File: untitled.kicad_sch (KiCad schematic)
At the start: 16 parts, among them J3 J_000001, J5 J_000002, U2 PWR_nPM1100-QDXX

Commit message: added test points
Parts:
- added TP1: TestPoint VDD, TestPoint:TestPoint_Pad_D1.5mm, symbol Connector:TestPoint
- added TP2: TestPoint GND, TestPoint:TestPoint_Pad_D1.5mm, symbol Connector:TestPoint
- added TP3: TestPoint VBAT, TestPoint:TestPoint_Pad_D1.5mm, symbol Connector:TestPoint
- added TP4: TestPoint VBUS, TestPoint:TestPoint_Pad_D1.5mm, symbol Connector:TestPoint
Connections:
- net +3V0 VDD_NRF: now also TP1.1
- net GND: now also TP2.1
- net VBAT: now also TP3.1
- net VBUS: now also TP4.1
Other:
- moved on the sheet: C17

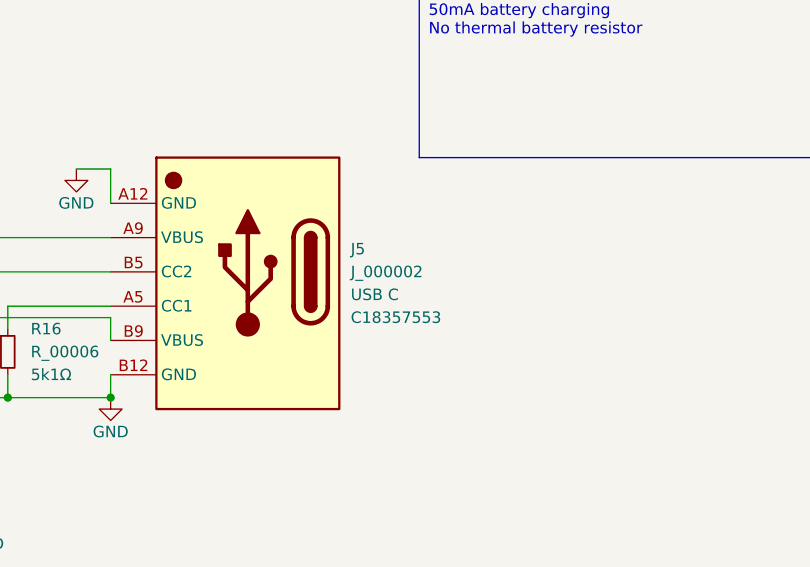
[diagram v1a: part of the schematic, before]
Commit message: fixed ERC errors
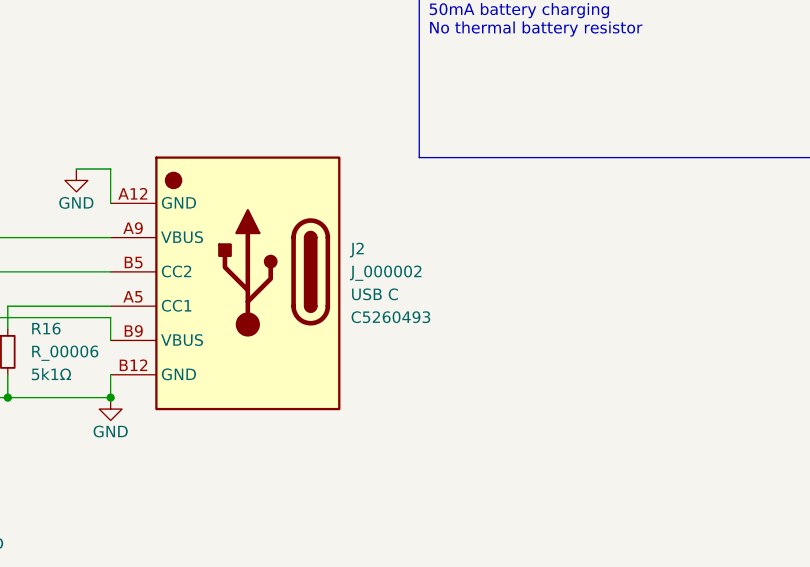
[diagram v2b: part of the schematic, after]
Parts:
- removed J5: J_000002, mic_patch_parts:C5260493, symbol mic_patch_parts:1000009
- added J2: J_000002, mic_patch_parts:J_000002, symbol mic_patch_parts:J_000002
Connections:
- net GND: now also J2.A12 (GND), J2.B12 (GND)
- net VBUS: now also J2.A9 (VBUS), J2.B9 (VBUS)
- net at R16.1: now also J2.A5 (CC1)
- net at R14.1: now also J2.B5 (CC2)
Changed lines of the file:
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@@
 	)
 	(symbol
-		(lib_id "mic_patch_parts:1000009")
+		(lib_id "mic_patch_parts:J_000002")
 		(at 193.04 62.23 0)
 		(unit 1)
@@
 		(dnp no)
 		(fields_autoplaced yes)
-		(property "Reference" "J5"
+		(property "Reference" "J2"
 			(at 207.01 55.8799 0)
 			(effects
@@
 			)
 		)
-		(property "Footprint" "mic_patch_parts:C5260493"
+		(property "Footprint" "mic_patch_parts:J_000002"
 			(at 194.564 78.232 0)
 			(effects
@@
 			)
 		)
-		(property "LCSC PNs" "C18357553"
+		(property "LCSC PNs" "C5260493"
 			(at 207.01 63.4999 0)
 			(effects
@@
 			)
 		)
+		(pin "A9"
+		)
+		(pin "B12"
+		)
 		(pin "B5"
+		)
+		(pin "B9"
 		)
 		(pin "A5"
@@
 		(pin "A12"
 		)
-		(pin "A9"
-		)
-		(pin "B12"
-		)
-		(pin "B12"
-		)
-		(pin "B9"
-		)
-		(pin "B9"
-		)
 		(instances
 			(project "mic_patch_v1"
 				(path "/5448a297-4261-40a5-8009-47199bfe22cb/549bd3f0-5402-4113-b11d-8a88b4fc0730"
-					(reference "J5")
+					(reference "J2")
 					(unit 1)
 				)

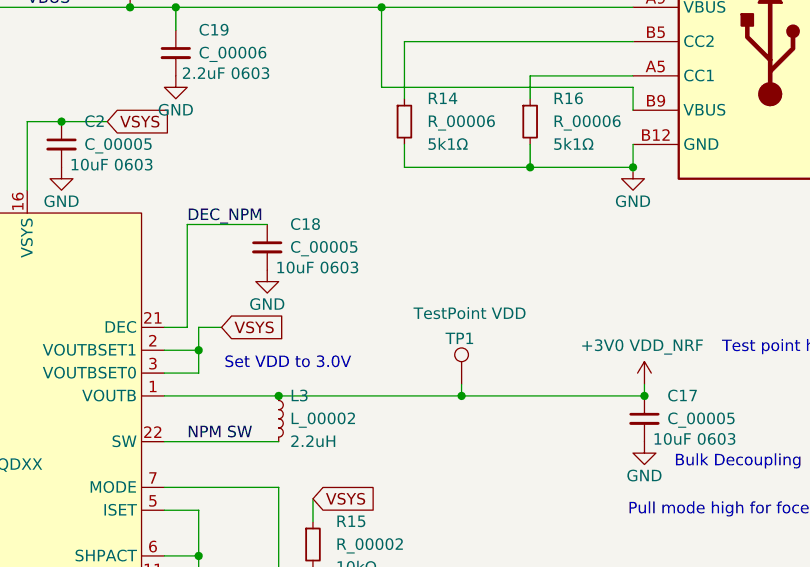
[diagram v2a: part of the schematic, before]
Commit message: poured ground layer added RF keep out
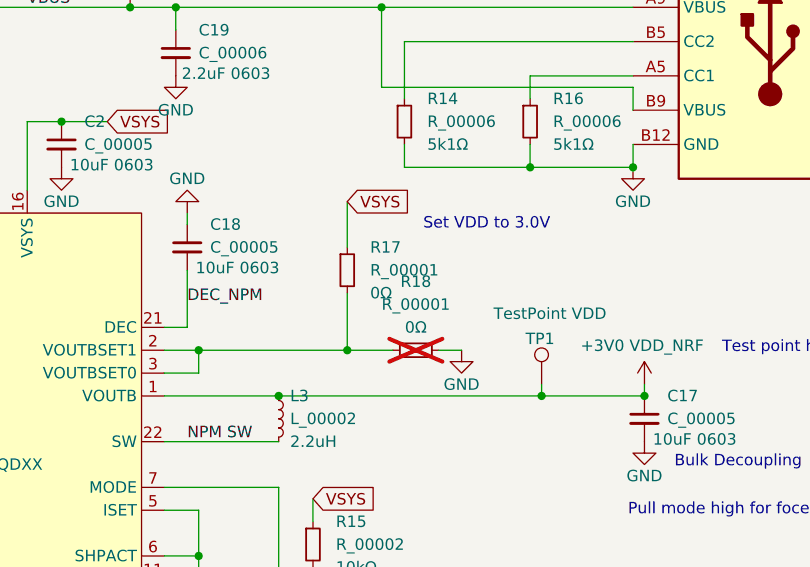
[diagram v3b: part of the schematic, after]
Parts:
- added R17, R18: R_00001, Resistor_SMD:R_0805_2012Metric, symbol mic_patch_parts:R_00001
- TP1, TP2, TP3, TP4: footprint TestPoint:TestPoint_Pad_D1.5mm -> TestPoint:TestPoint_Pad_D1.0mm
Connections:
- net DEC_NPM: now also C18.2; no longer C18.1
- net GND: now also C18.1, R18.1; no longer C18.2
- net VSYS: now also R17.1; no longer U2.2 (VOUTBSET1), U2.3 (VOUTBSET0)
- new net: R17.2, R18.2, U2.2 (VOUTBSET1), U2.3 (VOUTBSET0)
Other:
- moved on the sheet: C18, TP1

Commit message: re-routed buttons to closer pins
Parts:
- TP1, TP2: footprint TestPoint:TestPoint_Pad_D1.0mm -> TestPoint:TestPoint_Pad_D1.5mm
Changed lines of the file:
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@@
 			)
 		)
-		(property "Footprint" "TestPoint:TestPoint_Pad_D1.0mm"
+		(property "Footprint" "TestPoint:TestPoint_Pad_D1.5mm"
 			(at 175.26 96.52 0)
 			(effects
@@
 			)
 		)
-		(property "Footprint" "TestPoint:TestPoint_Pad_D1.0mm"
+		(property "Footprint" "TestPoint:TestPoint_Pad_D1.5mm"
 			(at 118.11 140.97 0)
 			(effects

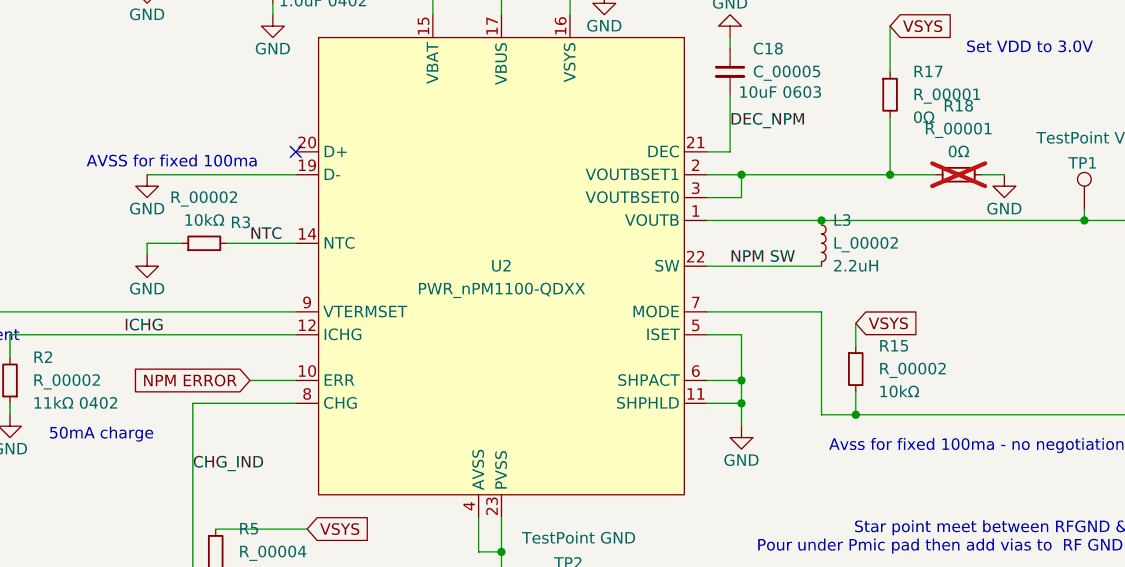
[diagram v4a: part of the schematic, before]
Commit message: corrected missing part numbers + inconsistencies
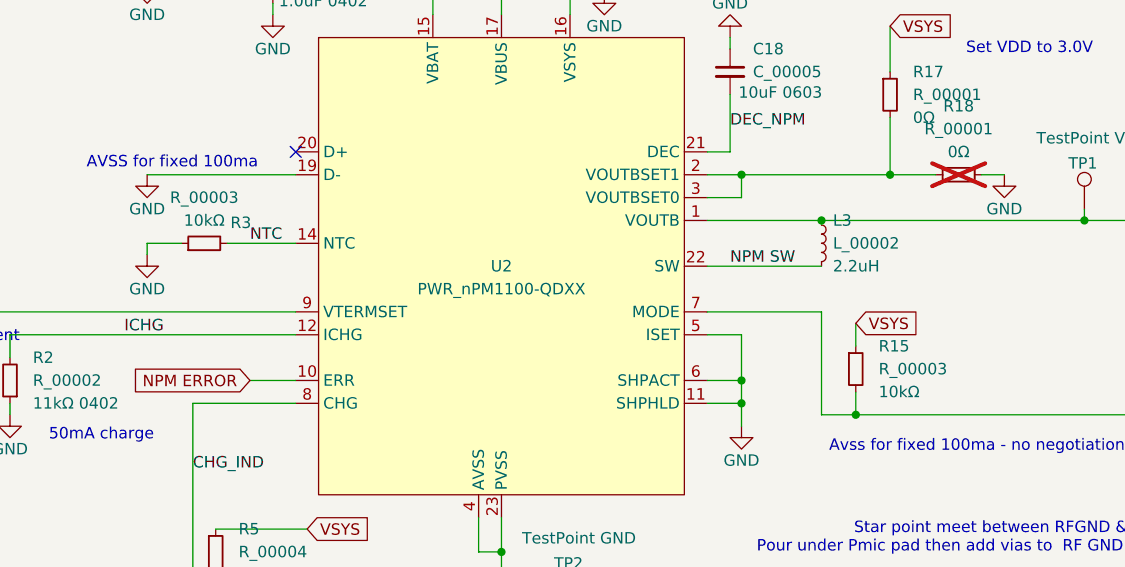
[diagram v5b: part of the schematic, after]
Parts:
- R15, R3: value R_00002 -> R_00003
- R17: LCSC PNs (none) -> C17477
- U2: LCSC PNs (none) -> C7249860
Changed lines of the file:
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@@
 	)
 	(symbol
+		(lib_name "R_00003_1")
 		(lib_id "mic_patch_parts:R_00003")
 		(at 144.78 114.3 0)
@@
 			)
 		)
-		(property "Value" "R_00002"
+		(property "Value" "R_00003"
 			(at 147.32 114.2999 0)
 			(effects
@@
 			)
 		)
-		(property "Value" "R_00002"
+		(property "Value" "R_00003"
 			(at 72.39 95.25 90)
 			(effects
@@
 			)
 		)
+		(property "LCSC PNs" "C7249860"
+			(at 105.41 102.87 0)
+			(effects
+				(font
+					(size 1.27 1.27)
+				)
+				(hide yes)
+			)
+		)
 		(pin "10"
 		)
@@
 	)
 	(symbol
+		(lib_name "R_00001_1")
 		(lib_id "mic_patch_parts:R_00001")
 		(at 148.59 83.82 0)
@@
 			)
 		)
-		(property "LCSC PNs" ""
+		(property "LCSC PNs" "C17477"
 			(at 148.59 83.82 0)
 			(effects

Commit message: updated footprint for C19, corrected
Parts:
- C19: footprint Capacitor_SMD:C_0201_0603Metric -> Capacitor_SMD:C_0603_1608Metric
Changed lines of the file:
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@@
 			)
 		)
-		(property "Footprint" "Capacitor_SMD:C_0201_0603Metric"
+		(property "Footprint" "Capacitor_SMD:C_0603_1608Metric"
 			(at 104.14 60.96 0)
 			(effects

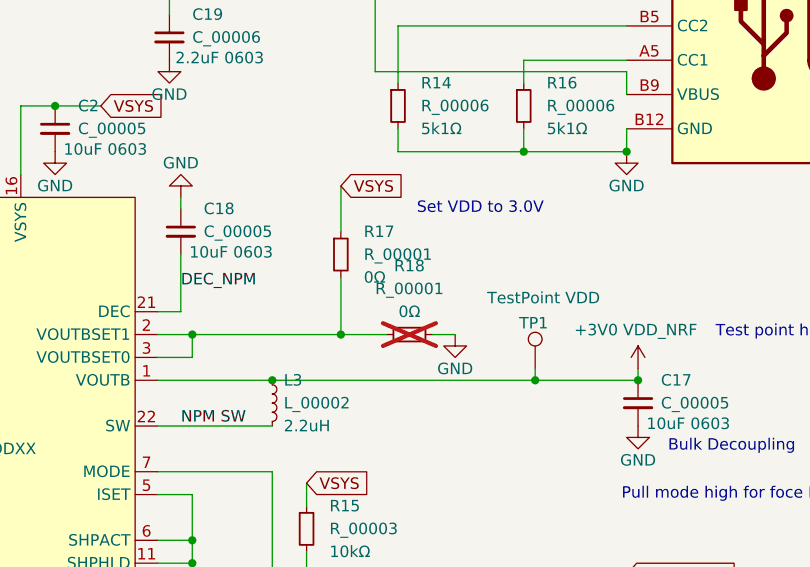
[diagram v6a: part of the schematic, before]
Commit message: Removed SD Card from schematic
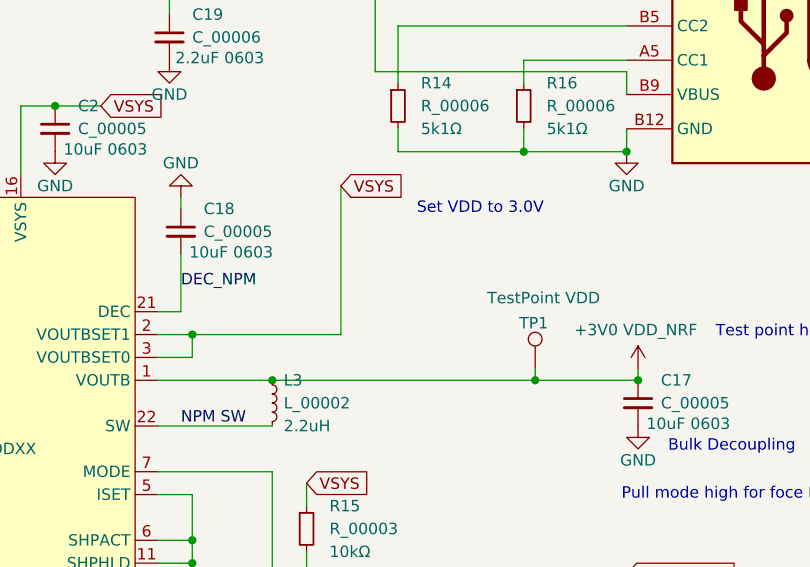
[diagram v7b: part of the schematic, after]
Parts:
- removed R17, R18: R_00001, Resistor_SMD:R_0805_2012Metric, symbol mic_patch_parts:R_00001
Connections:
- net VSYS: now also U2.2 (VOUTBSET1), U2.3 (VOUTBSET0)

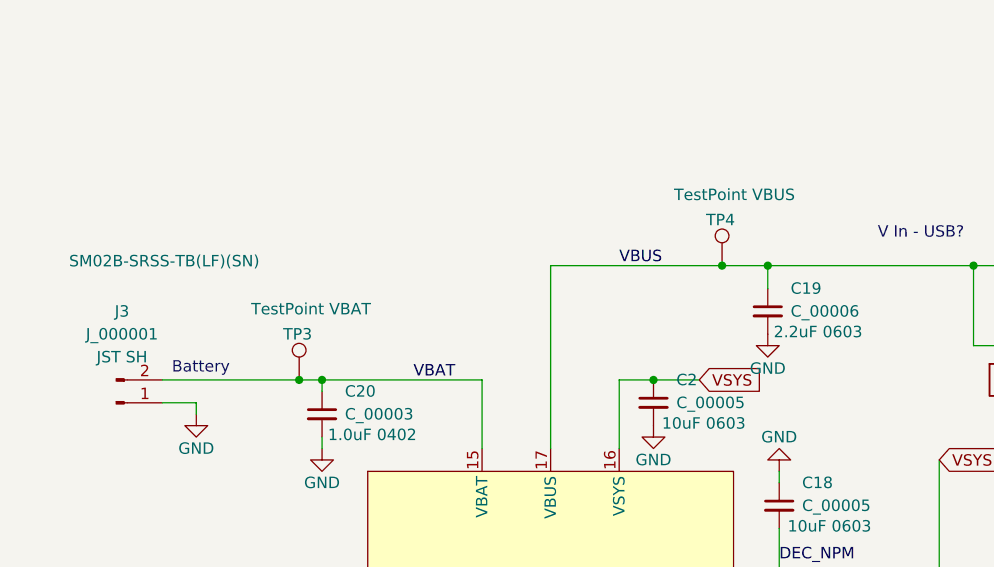
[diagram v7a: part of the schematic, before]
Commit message: Routed Power
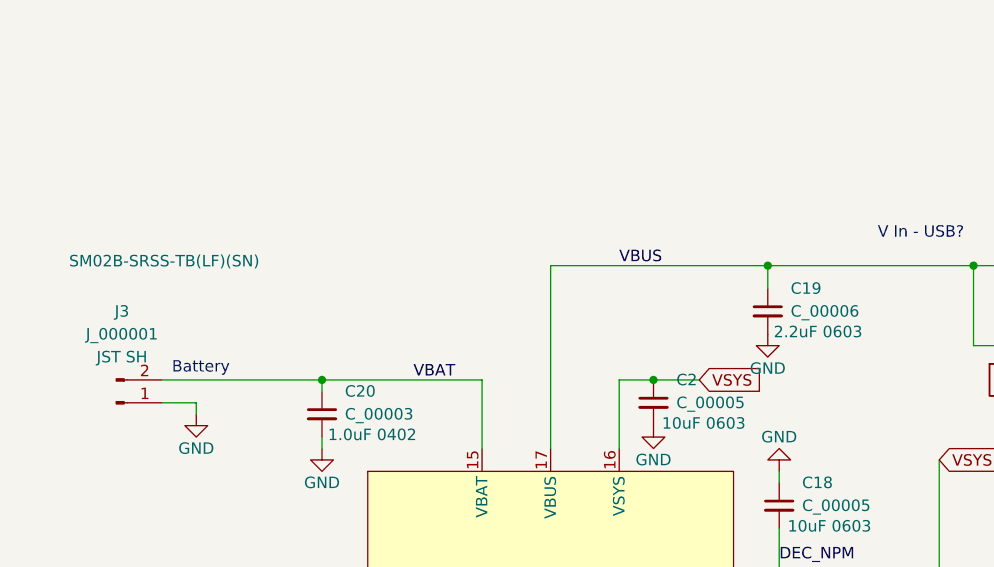
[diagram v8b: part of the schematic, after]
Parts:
- removed TP3: TestPoint VBAT, TestPoint:TestPoint_Pad_D1.0mm, symbol Connector:TestPoint
- removed TP4: TestPoint VBUS, TestPoint:TestPoint_Pad_D1.0mm, symbol Connector:TestPoint
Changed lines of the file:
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@@
-	)
-	(junction
-		(at 124.46 54.61)
-		(diameter 0)
-		(color 0 0 0 0)
 	)
 	(junction
@@
 	)
 	(junction
-		(at 77.47 67.31)
-		(diameter 0)
-		(color 0 0 0 0)
-	)
-	(junction
 		(at 132.08 92.71)
 		(diameter 0)
@@
 	(wire
 		(pts
-			(xy 77.47 67.31) (xy 80.01 67.31)
+			(xy 62.23 67.31) (xy 80.01 67.31)
 		)
 		(stroke
@@
 	(wire
 		(pts
-			(xy 124.46 54.61) (xy 129.54 54.61)
-		)
-		(stroke
-			(width 0)
-			(type default)
-		)
-	)
-	(wire
-		(pts
 			(xy 43.18 107.95) (xy 82.55 107.95)
 		)
@@
 	(wire
 		(pts
-			(xy 62.23 67.31) (xy 77.47 67.31)
-		)
-		(stroke
-			(width 0)
-			(type default)
-		)
-	)
-	(wire
-		(pts
 			(xy 50.8 110.49) (xy 82.55 110.49)
 		)
@@
 	(wire
 		(pts
-			(xy 105.41 54.61) (xy 124.46 54.61)
+			(xy 105.41 54.61) (xy 129.54 54.61)
 		)
 		(stroke
@@
 	)
 	(symbol
-		(lib_id "Connector:TestPoint")
-		(at 124.46 54.61 0)
-		(unit 1)
-		(exclude_from_sim no)
-		(in_bom yes)
-		(on_board yes)
-		(dnp no)
-		(property "Reference" "TP4"
-			(at 122.682 49.53 0)
-			(effects
-				(font
-					(size 1.27 1.27)
-				)
-				(justify left)
-			)
-		)
-		(property "Value" "TestPoint VBUS"
-			(at 119.126 46.736 0)
-			(effects
-				(font
-					(size 1.27 1.27)
-				)
-				(justify left)
-			)
-		)
-		(property "Footprint" "TestPoint:TestPoint_Pad_D1.0mm"
-			(at 129.54 54.61 0)
-			(effects
-				(font
-					(size 1.27 1.27)
-				)
-				(hide yes)
-			)
-		)
-		(property "Datasheet" "~"
-			(at 129.54 54.61 0)
-			(effects
-				(font
-					(size 1.27 1.27)
-				)
-				(hide yes)
-			)
-		)
-		(property "Description" "test point"
-			(at 124.46 54.61 0)
-			(effects
-				(font
-					(size 1.27 1.27)
-				)
-				(hide yes)
-			)
-		)
-		(pin "1"
-		)
-		(instances
-			(project "mic_patch_v1"
-				(path "/5448a297-4261-40a5-8009-47199bfe22cb/549bd3f0-5402-4113-b11d-8a88b4fc0730"
-					(reference "TP4")
-					(unit 1)
-				)
-			)
-		)
-	)
-	(symbol
 		(lib_id "mic_patch_parts:R_00002")
 		(at 50.8 115.57 180)
@@
 					(unit 1)
 				)
-			)
-		)
-	)
-	(symbol
-		(lib_id "Connector:TestPoint")
-		(at 77.47 67.31 0)
-		(unit 1)
-		(exclude_from_sim no)
-		(in_bom yes)
-		(on_board yes)
-		(dnp no)
-		(property "Reference" "TP3"
-			(at 75.692 62.23 0)
-			(effects
-				(font
-					(size 1.27 1.27)
-				)
-				(justify left)
-			)
-		)
-		(property "Value" "TestPoint VBAT"
-			(at 72.136 59.436 0)
-			(effects
-				(font
-					(size 1.27 1.27)
-				)
-				(justify left)
-			)
-		)
-		(property "Footprint" "TestPoint:TestPoint_Pad_D1.0mm"
-			(at 82.55 67.31 0)
-			(effects
-				(font
-					(size 1.27 1.27)
-				)
-				(hide yes)
-			)
-		)
-		(property "Datasheet" "~"
-			(at 82.55 67.31 0)
-			(effects
-				(font
-					(size 1.27 1.27)
-				)
-				(hide yes)
-			)
-		)
-		(property "Description" "test point"
-			(at 77.47 67.31 0)
-			(effects
-				(font
-					(size 1.27 1.27)
-				)
-				(hide yes)
-			)
-		)
-		(pin "1"
-		)
-		(instances
-			(project "mic_patch_v1"
-				(path "/5448a297-4261-40a5-8009-47199bfe22cb/549bd3f0-5402-4113-b11d-8a88b4fc0730"
-					(reference "TP3")
-					(unit 1)
-				)
